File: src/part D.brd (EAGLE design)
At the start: 41 x 75.5 mm, 1 part

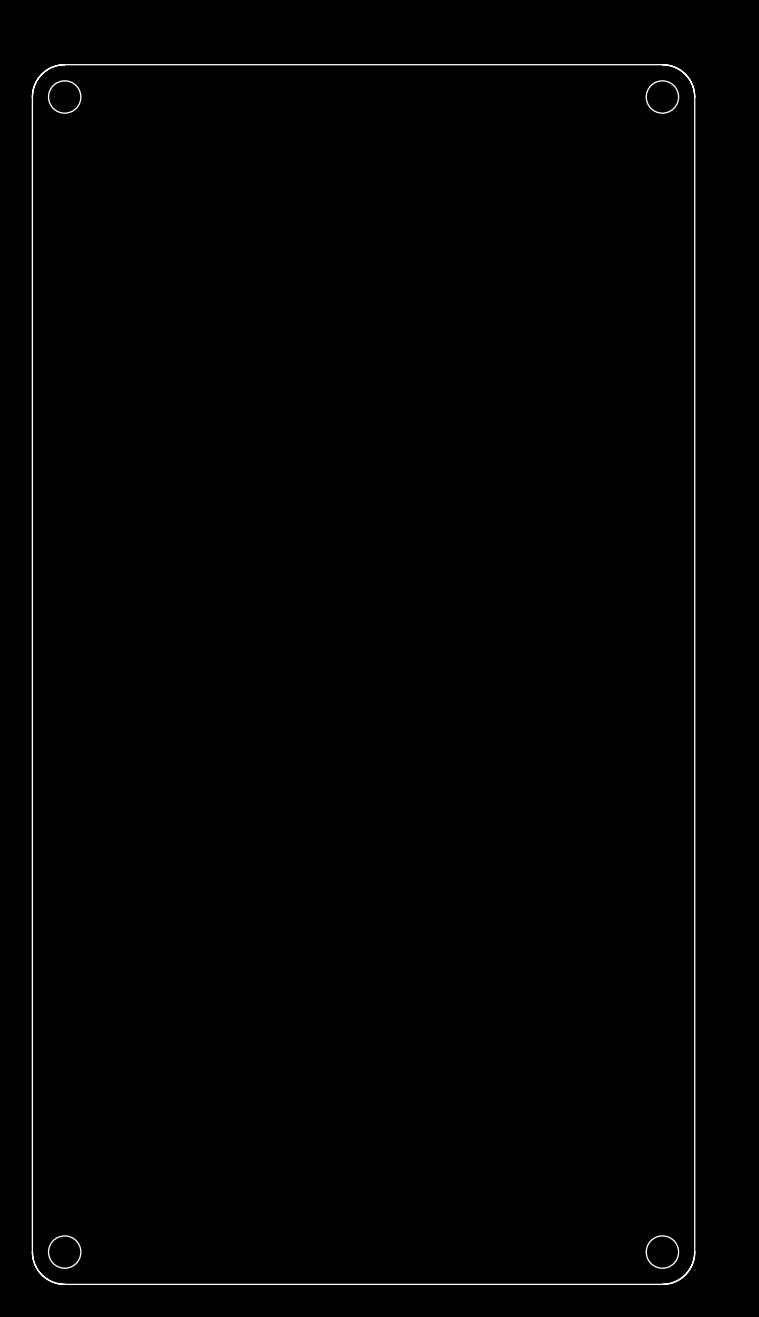
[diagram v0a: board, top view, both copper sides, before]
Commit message: CAN bus voltage measurement implemented #29 (#32)
* CAN bus voltage measurement implemented #29

* CAN_VDD_EN pulled up to 5v #28

* #31 #30 #9

* ready for review

* minor changes

* version text added

* update readme
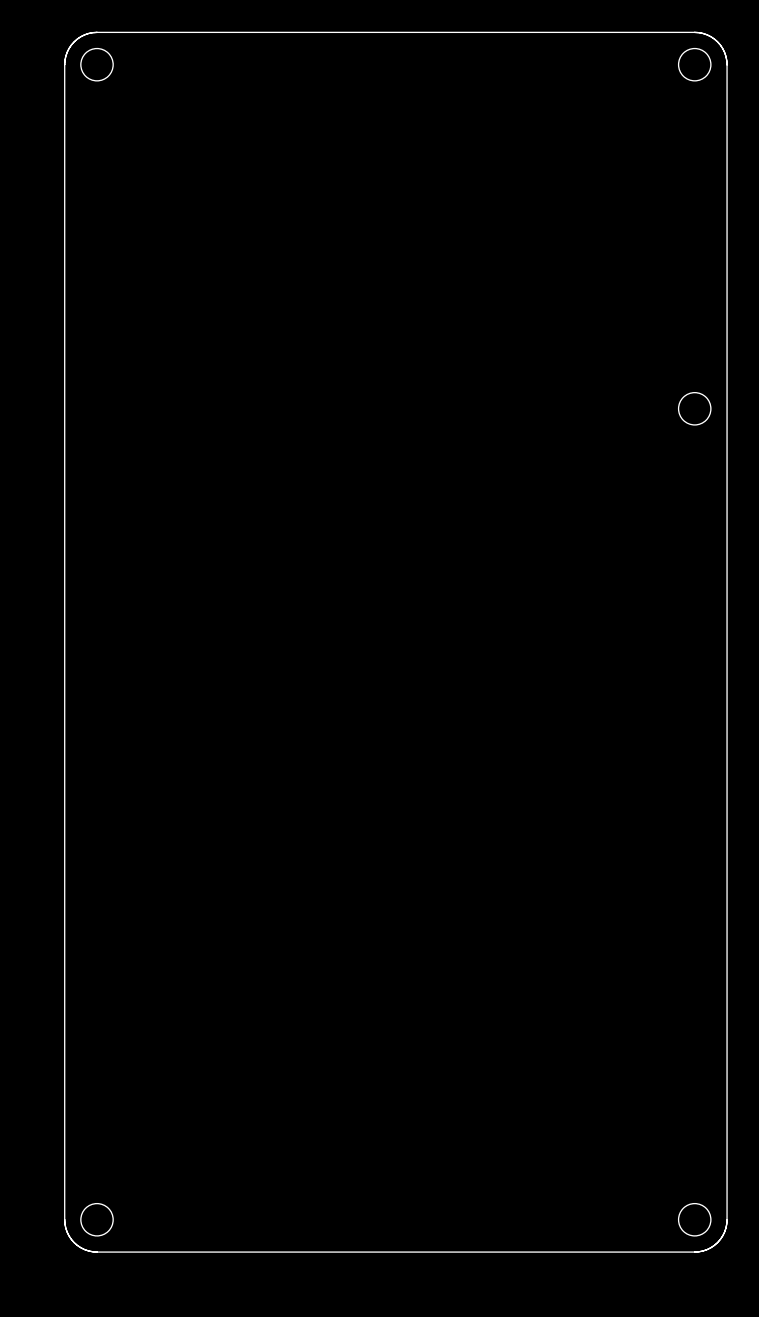
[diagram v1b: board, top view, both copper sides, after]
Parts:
- moved E$1 2.83 mm to (10.5, 14.5)
